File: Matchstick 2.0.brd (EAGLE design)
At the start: 73 x 38 mm, 13 parts, among them IC1 74HCT125D, J1 694106301002, J2 TARGET, J3 691241510006, J4 691241510006, U1 M5STAMP PICO

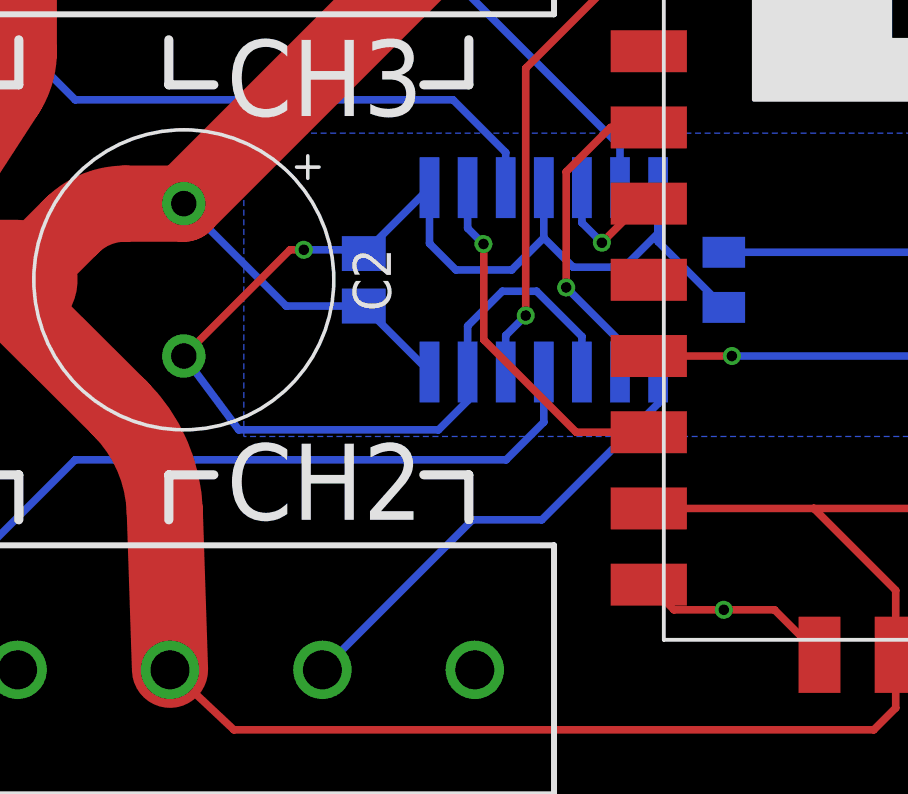
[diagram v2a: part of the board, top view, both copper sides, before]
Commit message: fixing the crossed signals
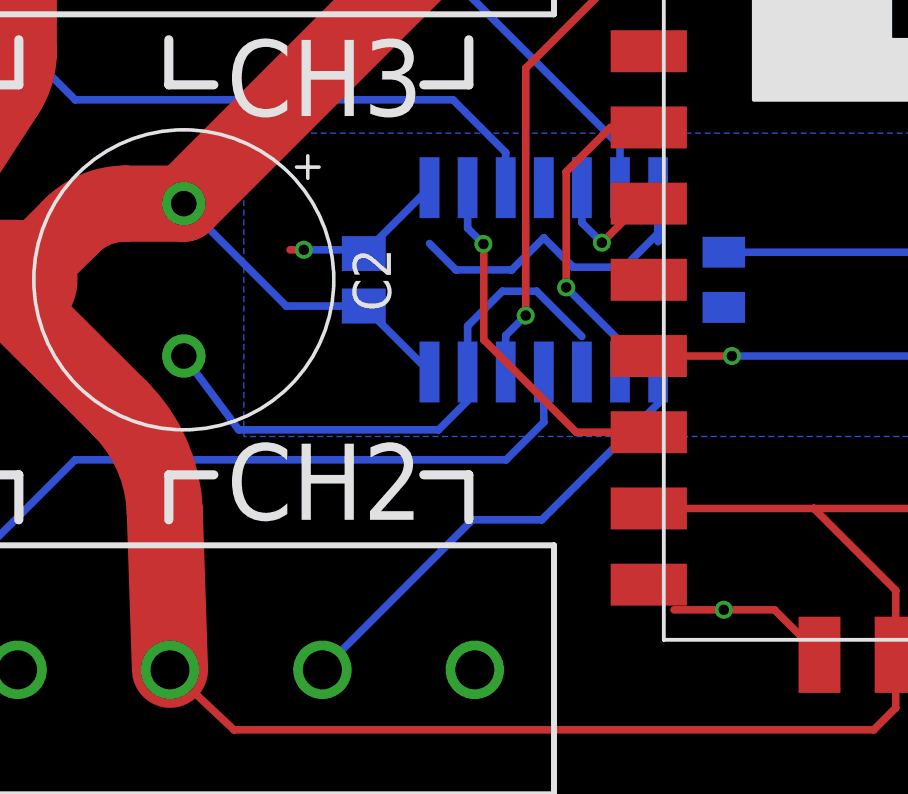
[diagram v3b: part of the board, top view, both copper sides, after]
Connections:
- new net GND: C2.2, IC1.1, IC1.10, IC1.13, IC1.4, J1.2, J2.P$6, J3.3, J3.6, J4.3, J4.6, R1.2, R2.1, S1.1, U1.10, U1.14, U1.9
- net STATUS_LED$2: no longer C2.2, IC1.1, IC1.10, IC1.13, IC1.4, J1.2, J2.P$6, J3.3, J3.6, J4.3, J4.6, R1.2, R2.1, S1.1, U1.10, U1.14, U1.9
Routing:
- net STATUS_LED$2: track 62.4 -> 18.2 mm, vias 5 -> 1
- net GND: track 0.00 -> 29.2 mm, vias 0 -> 4
- added copper zone on layer 16, net GND
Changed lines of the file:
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@@
 <signals>
 <signal name="STATUS_LED$2">
-<contactref element="U1" pad="9"/>
-<contactref element="J2" pad="P$6"/>
-<contactref element="S1" pad="1"/>
-<contactref element="U1" pad="10"/>
-<contactref element="U1" pad="14"/>
-<contactref element="R1" pad="2"/>
-<contactref element="IC1" pad="1"/>
-<contactref element="IC1" pad="4"/>
 <contactref element="IC1" pad="7"/>
 <contactref element="C1" pad="2"/>
-<contactref element="IC1" pad="10"/>
-<contactref element="IC1" pad="13"/>
-<contactref element="J1" pad="2"/>
-<contactref element="R2" pad="1"/>
-<contactref element="J3" pad="3"/>
-<contactref element="J4" pad="3"/>
-<contactref element="C2" pad="2"/>
-<contactref element="J3" pad="6"/>
-<contactref element="J4" pad="6"/>
-<polygon width="0.254" layer="16" isolate="1.016">
-<vertex x="0" y="0"/>
-<vertex x="73" y="0"/>
-<vertex x="73" y="38"/>
-<vertex x="0" y="38"/>
-<vertex x="0" y="24"/>
-<vertex x="5" y="24"/>
-<vertex x="5" y="14"/>
-<vertex x="0" y="14"/>
-</polygon>
-<via x="39" y="8" extent="1-16" drill="0.35"/>
-<via x="58" y="8" extent="1-16" drill="0.35"/>
-<via x="61" y="30" extent="1-16" drill="0.35"/>
-<via x="68" y="2" extent="1-16" drill="0.35"/>
-<wire x1="29.492" y1="14" x2="22.83" y2="14" width="0.254" layer="16"/>
-<wire x1="22.83" y1="14" x2="21" y2="16.46" width="0.254" layer="16"/>
 <polygon width="0.254" layer="16" pour="cutout">
 <vertex x="23" y="23.889"/>
@@
 <vertex x="23" y="13.778"/>
 </polygon>
-<wire x1="65.794" y1="2.095" x2="67.905" y2="2.095" width="0.254" layer="1"/>
-<wire x1="67.905" y1="2.095" x2="68" y2="2" width="0.254" layer="1"/>
-<wire x1="62.0805" y1="30" x2="61" y2="30" width="0.254" layer="1"/>
-<wire x1="39" y1="8" x2="37.34" y2="8" width="0.254" layer="1"/>
-<wire x1="37.34" y1="8" x2="36.5" y2="8.84" width="0.254" layer="1"/>
-<wire x1="39" y1="8" x2="40.69" y2="8" width="0.254" layer="1"/>
-<wire x1="40.69" y1="8" x2="42.19" y2="6.5" width="0.254" layer="1"/>
-<wire x1="55.5" y1="8.84" x2="57.16" y2="8.84" width="0.254" layer="1"/>
-<wire x1="57.16" y1="8.84" x2="58" y2="8" width="0.254" layer="1"/>
-<wire x1="30.46" y1="15.9266" x2="30.46" y2="14.968" width="0.254" layer="16"/>
-<wire x1="30.46" y1="14.968" x2="29.492" y2="14" width="0.254" layer="16"/>
-<wire x1="30.46" y1="15.9266" x2="30.46" y2="17.46" width="0.254" layer="16"/>
-<wire x1="30.46" y1="17.46" x2="31.619" y2="18.619" width="0.254" layer="16"/>
-<wire x1="31.619" y1="18.619" x2="32.762" y2="18.619" width="0.254" layer="16"/>
-<wire x1="32.762" y1="18.619" x2="34.27" y2="17.111" width="0.254" layer="16"/>
-<wire x1="34.27" y1="17.111" x2="34.27" y2="15.9266" width="0.254" layer="16"/>
 <wire x1="29.19" y1="20.21" x2="30.069" y2="19.331" width="0.254" layer="16"/>
 <wire x1="30.069" y1="19.331" x2="31.931" y2="19.331" width="0.254" layer="16"/>
 <wire x1="33" y1="20.4" x2="31.931" y2="19.331" width="0.254" layer="16"/>
 <wire x1="27" y1="19.8754" x2="29.19" y2="22.0654" width="0.254" layer="16"/>
-<wire x1="29.19" y1="22.0654" x2="29.19" y2="22.0734" width="0.508" layer="16"/>
 <via x="25" y="20" extent="1-16" drill="0.35"/>
-<wire x1="21" y1="16.46" x2="24.54" y2="20" width="0.254" layer="1"/>
 <wire x1="24.54" y1="20" x2="25" y2="20" width="0.254" layer="1"/>
 <wire x1="25" y1="20" x2="26.8754" y2="20" width="0.254" layer="16"/>
 <wire x1="26.8754" y1="20" x2="27" y2="19.8754" width="0.508" layer="16"/>
 <wire x1="36.81" y1="20.554" x2="36.81" y2="22.0734" width="0.254" layer="16"/>
-<polygon width="1.27" layer="16" isolate="1.016">
-<vertex x="0" y="24"/>
-<vertex x="5" y="24"/>
-<vertex x="5" y="14"/>
-<vertex x="0" y="14"/>
-</polygon>
 <wire x1="35.678" y1="19.422" x2="36.81" y2="20.554" width="0.254" layer="16"/>
-<wire x1="29.19" y1="22.0734" x2="29.19" y2="20.21" width="0.254" layer="16"/>
-<wire x1="33" y1="22.0734" x2="33" y2="20.4" width="0.254" layer="16"/>
 <wire x1="33" y1="20.4" x2="33.978" y2="19.422" width="0.254" layer="16"/>
 <wire x1="33.978" y1="19.422" x2="35.678" y2="19.422" width="0.254" layer="16"/>
 <wire x1="36.81" y1="22.0734" x2="36.81" y2="20.2705" width="0.254" layer="16"/>
-<wire x1="36.81" y1="20.2705" x2="39" y2="18.0805" width="0.254" layer="16"/>
+<wire x1="29.19" y1="22.0654" x2="29.19" y2="20.21" width="0" layer="19" extent="16-16"/>
 </signal>
 <signal name="DATA$4">
@@
 <wire x1="35.54" y1="23.46" x2="27" y2="32" width="0.254" layer="16"/>
 </signal>
+<signal name="GND">
+<contactref element="IC1" pad="1"/>
+<contactref element="IC1" pad="10"/>
+<contactref element="IC1" pad="13"/>
+<wire x1="30.46" y1="15.9266" x2="30.46" y2="17.46" width="0.254" layer="16"/>
+<wire x1="30.46" y1="17.46" x2="31.619" y2="18.619" width="0.254" layer="16"/>
+<wire x1="31.619" y1="18.619" x2="32.762" y2="18.619" width="0.254" layer="16"/>
+<wire x1="32.762" y1="18.619" x2="34.27" y2="17.111" width="0.254" layer="16"/>
+<contactref element="IC1" pad="4"/>
+<contactref element="J1" pad="2"/>
+<contactref element="C2" pad="2"/>
+<wire x1="29.492" y1="14" x2="22.83" y2="14" width="0.254" layer="16"/>
+<wire x1="22.83" y1="14" x2="21" y2="16.46" width="0.254" layer="16"/>
+<wire x1="30.46" y1="14.968" x2="29.492" y2="14" width="0.254" layer="16"/>
+<contactref element="R1" pad="2"/>
+<contactref element="S1" pad="1"/>
+<via x="68" y="2" extent="1-16" drill="0.35"/>
+<wire x1="65.794" y1="2.095" x2="67.905" y2="2.095" width="0.254" layer="1"/>
+<wire x1="67.905" y1="2.095" x2="68" y2="2" width="0.254" layer="1"/>
+<contactref element="J2" pad="P$6"/>
+<contactref element="R2" pad="1"/>
+<via x="61" y="30" extent="1-16" drill="0.35"/>
+<wire x1="62.0805" y1="30" x2="61" y2="30" width="0.254" layer="1"/>
+<contactref element="J4" pad="6"/>
+<contactref element="J4" pad="3"/>
+<contactref element="J3" pad="6"/>
+<contactref element="J3" pad="3"/>
+<contactref element="U1" pad="9"/>
+<contactref element="U1" pad="10"/>
+<via x="39" y="8" extent="1-16" drill="0.35"/>
+<wire x1="39" y1="8" x2="37.34" y2="8" width="0.254" layer="1"/>
+<wire x1="39" y1="8" x2="40.69" y2="8" width="0.254" layer="1"/>
+<wire x1="40.69" y1="8" x2="42.19" y2="6.5" width="0.254" layer="1"/>
+<contactref element="U1" pad="14"/>
+<via x="58" y="8" extent="1-16" drill="0.35"/>
+<wire x1="55.5" y1="8.84" x2="57.16" y2="8.84" width="0.254" layer="1"/>
+<wire x1="57.16" y1="8.84" x2="58" y2="8" width="0.254" layer="1"/>
+<polygon width="0.254" layer="16" isolate="1.016">
+<vertex x="0" y="0"/>
+<vertex x="73" y="0"/>
+<vertex x="73" y="38"/>
+<vertex x="0" y="38"/>
+<vertex x="0" y="24"/>
+<vertex x="5" y="24"/>
+<vertex x="5" y="14"/>
+<vertex x="0" y="14"/>
+</polygon>
+<polygon width="1.27" layer="16" isolate="1.016">
+<vertex x="0" y="24"/>
+<vertex x="5" y="24"/>
+<vertex x="5" y="14"/>
+<vertex x="0" y="14"/>
+</polygon>
+<wire x1="34.27" y1="17.111" x2="39" y2="18.0805" width="0" layer="19" extent="16-16"/>
+<wire x1="30.46" y1="14.968" x2="30.46" y2="15.9266" width="0" layer="19" extent="16-16"/>
+<wire x1="34.27" y1="15.9266" x2="34.27" y2="17.111" width="0" layer="19" extent="16-16"/>
+<wire x1="36.5" y1="8.84" x2="37.34" y2="8" width="0" layer="19" extent="1-1"/>
+<wire x1="33" y1="22.0734" x2="34.27" y2="17.111" width="0" layer="19" extent="16-16"/>
+<wire x1="29.19" y1="22.0734" x2="33" y2="22.0734" width="0" layer="19" extent="16-16"/>
+</signal>
 </signals>

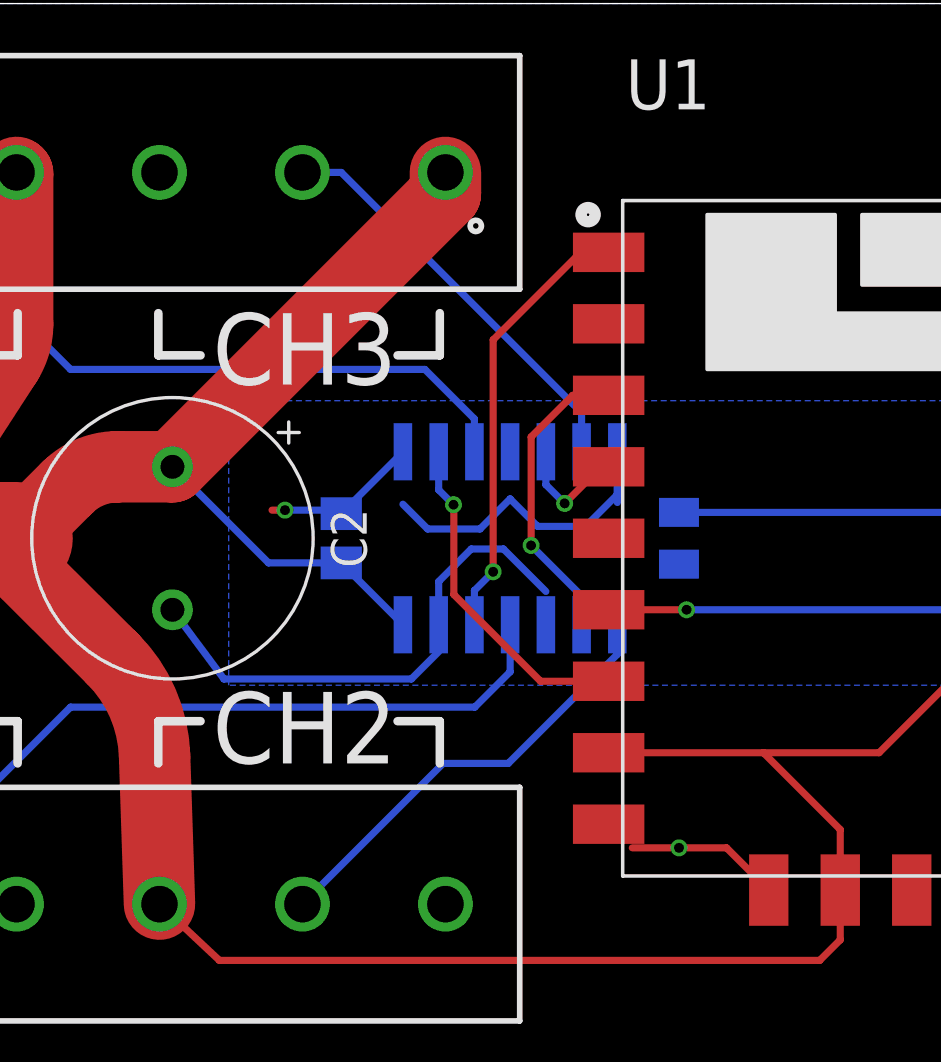
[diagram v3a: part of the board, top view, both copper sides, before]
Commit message: fixing the crossed signals 2
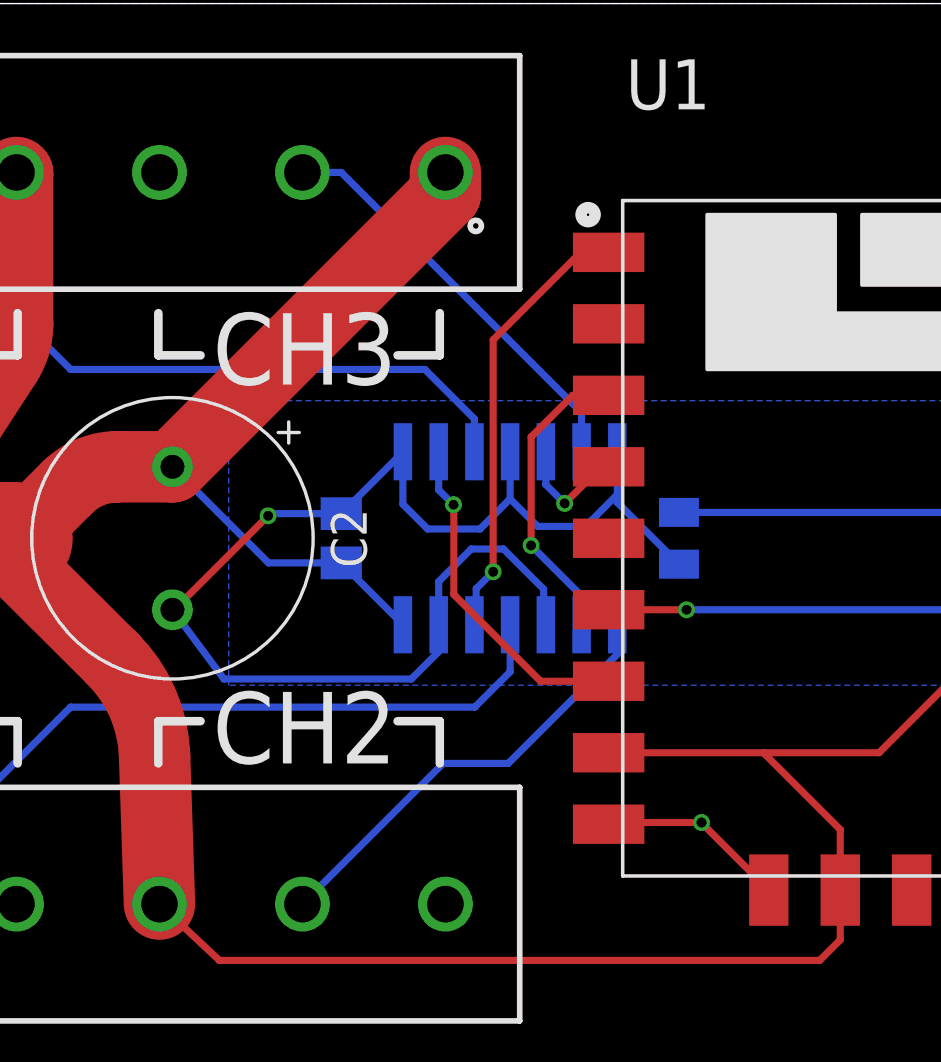
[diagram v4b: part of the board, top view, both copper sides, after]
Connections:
- removed net STATUS_LED$2: C1.2, IC1.7
- net GND: now also C1.2, IC1.7
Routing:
- net GND: track 29.2 -> 60.8 mm, vias 4 -> 5
- net STATUS_LED$2: track 18.2 -> 0.00 mm, vias 1 -> 0
- removed copper zone on layer 16, net STATUS_LED$2
